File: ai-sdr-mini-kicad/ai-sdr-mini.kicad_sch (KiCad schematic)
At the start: 62 parts, among them J1 KH-TYPE-C-6P, SW1 RESET, U1 USB2514B, U2 SI4732, U3 TMAG5273, U4 ESP32-S3-N8R8, U5 BMI260, U6 ATGM336H, U7 AMS1117-3.3, X1 32.768kHz, X2 24MHz

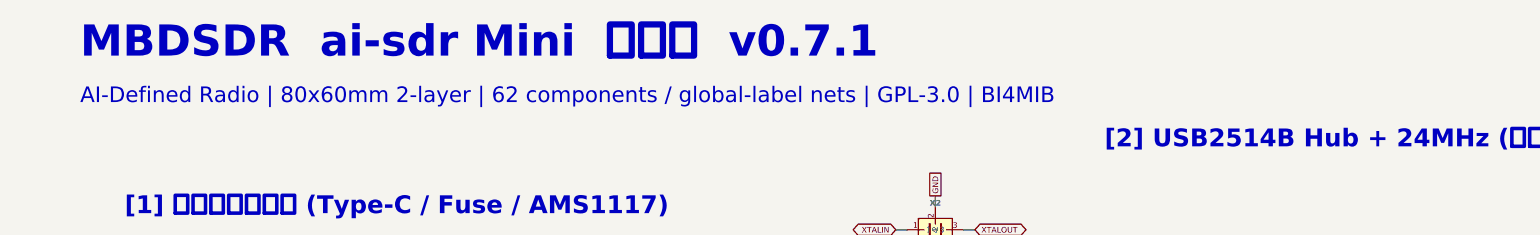
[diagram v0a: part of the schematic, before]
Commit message: chore: 身份脱敏——呼号/城市字面量全库中性化 + AGENTS.md 协作规则
公开仓库只放作品。全库扫描并替换身份字面量（测试全绿后提交）：

- 呼号 -> 中性示例呼号（同为合法格式，各端 roundtrip fixtures 自洽）：
  77 个文件，含协议测试夹具（ft8/ax25/fldigi/ssdv smoke）、KiCad 工程、
  文档、tool_param_smoke_result.json；
- 城市/站点标签 -> 中性表述（示例站/示例坐标/示例城市）：含 astronomy/
  satellite/pose 的站点注释、audit_r2 缺陷描述、实验 prompt、UI mockup
  地图标签（连同城区名）。测试夹具的数值坐标不动——它们同时是
  test_no_sim_regression / test_new_spacetime_panel 两条"禁止硬编码
  坐标"红线测试的对照数据，擅动会连锁破坏期望值；
- 新文件 AGENTS.md：身份红线（禁姓名/呼号/就学/城市/联系方式/浮动能力
  数字）、诚实文化、工程约定（单一事实源/四道门/_TOOL_DOMAIN 登记）、
  Windows 施工纪律（-F 消息文件、token 不落盘）、测试基线。author 元数据
  按作者此前明确要求保持归一身份（贡献图谱可归属），属账号层例外，
  AGENTS.md 只登记规则不写具体值。

未处理（如实登记）：cpp/tests/lrpt_e2e_iq.raw 为二进制 RS 编码 fixture，
呼号嵌在 FEC 帧内，盲改字节会破坏校验且本机 C++ 工具链不可用——需在
健康工具链上重新生成该 fixture 后再脱敏。

验证：python3 -m pytest mbdsdr_ai/tests -q -> 564 passed / 10 skipped
（与替换前一致，零退步）。
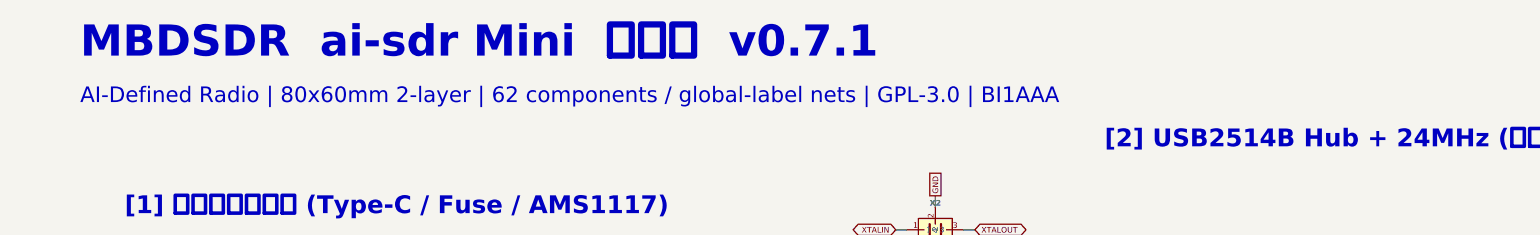
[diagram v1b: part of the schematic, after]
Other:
- note added: "AI-Defined Radio | 80x60mm 2-layer | 62 components / global-label nets | GPL-3.0 | BI1AAA"
- note removed: "AI-Defined Radio | 80x60mm 2-layer | 62 components / global-label nets | GPL-3.0 | BI4MIB"
- company: MBDSDR Open Source Project (BI4MIB) -> MBDSDR Open Source Project (BI1AAA)
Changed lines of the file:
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@@
     (date "2026-09-16")
     (rev "v0.7.1")
-    (company "MBDSDR Open Source Project (BI4MIB)")
+    (company "MBDSDR Open Source Project (BI1AAA)")
     (comment 1 "Complete v0.7.1 schematic, global-label nets, auto-routable")
     (comment 2 "GPL-3.0 License")
@@
   )
   (text
-    "AI-Defined Radio | 80x60mm 2-layer | 62 components / global-label nets | GPL-3.0 | BI4MIB"
+    "AI-Defined Radio | 80x60mm 2-layer | 62 components / global-label nets | GPL-3.0 | BI1AAA"
     (at 20 30 0)
     (effects
